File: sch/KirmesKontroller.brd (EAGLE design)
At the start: 100 x 80 mm, 31 parts, among them IC1 R-78E05-1.0, IC2 YB-ESP32-S3-AMP-V2, IC3 ULN2803, J1 MPE 087-1-003, X1 DG240 2,54-2, X2 DG240 2,54-2, X3 DG240 2,54-8, X4 DG240 2,54-8, X5 22-23-2031, X6 22-23-2031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

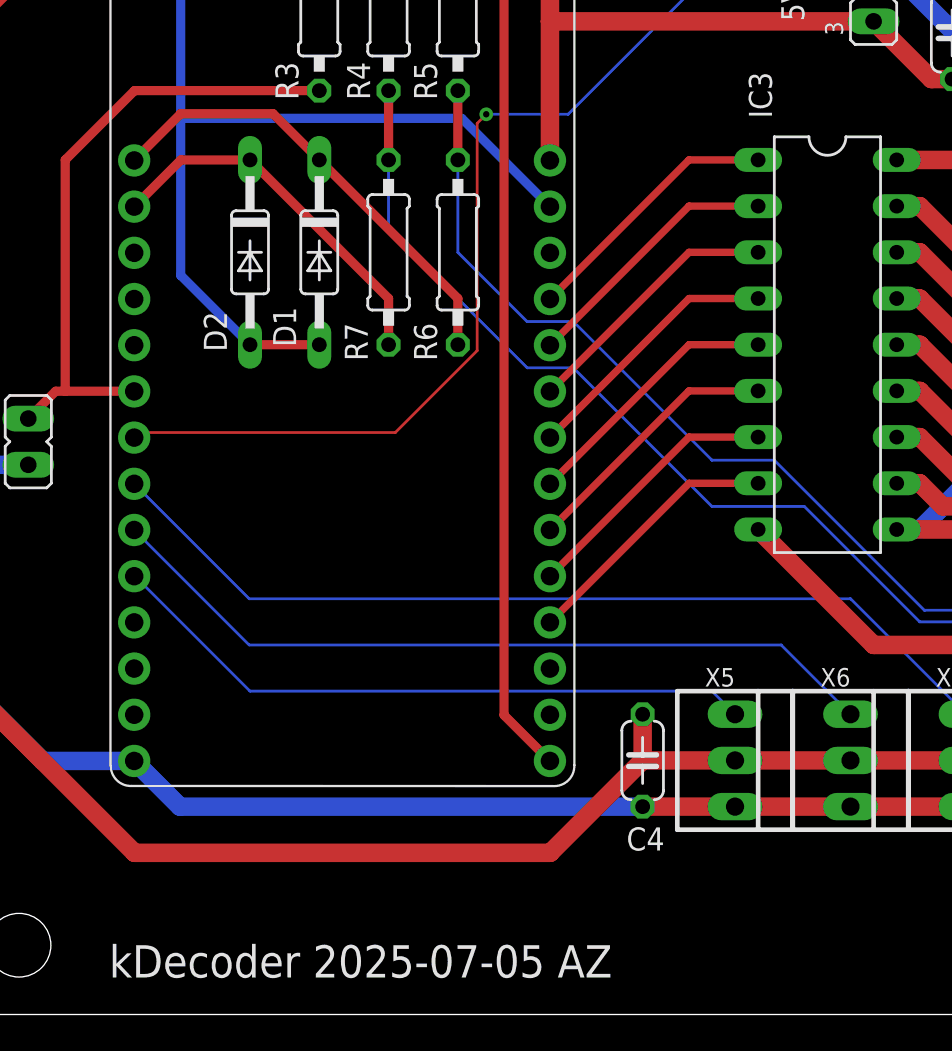
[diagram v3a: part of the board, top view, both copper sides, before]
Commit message: fixed pinmapping
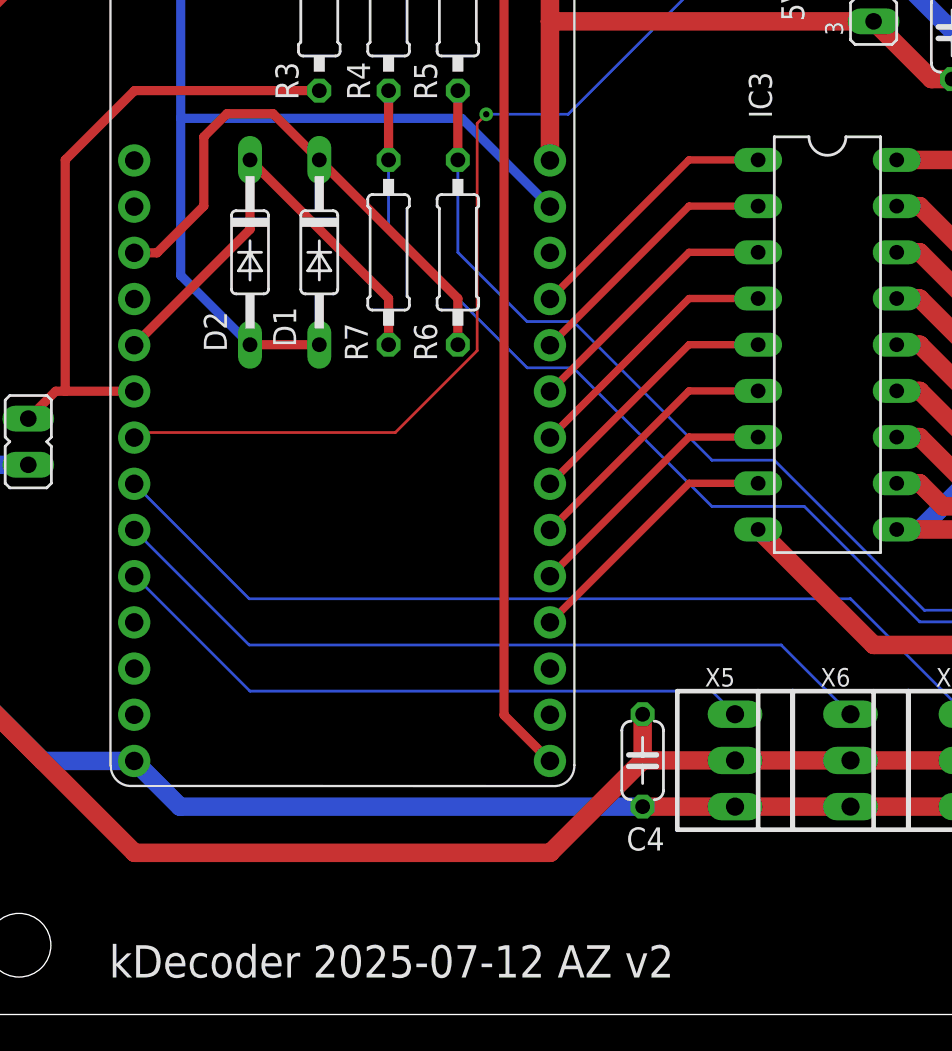
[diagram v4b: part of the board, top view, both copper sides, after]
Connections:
- net INPUT1: now also IC2.21; no longer IC2.47
- net INPUT2: now also IC2.38; no longer IC2.48
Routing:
- net INPUT2: track 20.7 -> 26.1 mm
- net INPUT1: track 25.6 -> 29.9 mm
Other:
- board text added: "kDecoder 2025-07-12 AZ v2"
- board text removed: "kDecoder 2025-07-05 AZ"
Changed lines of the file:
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@@
 <layers>
 <layer number="1" name="Top" color="4" fill="1" visible="yes" active="yes"/>
-<layer number="16" name="Bottom" color="1" fill="1" visible="yes" active="yes"/>
+<layer number="16" name="Bottom" color="1" fill="1" visible="no" active="yes"/>
 <layer number="17" name="Pads" color="2" fill="1" visible="yes" active="yes"/>
 <layer number="18" name="Vias" color="2" fill="1" visible="yes" active="yes"/>
@@
 <layer number="20" name="Dimension" color="24" fill="1" visible="yes" active="yes"/>
 <layer number="21" name="tPlace" color="7" fill="1" visible="yes" active="yes"/>
-<layer number="22" name="bPlace" color="7" fill="1" visible="yes" active="yes"/>
+<layer number="22" name="bPlace" color="7" fill="1" visible="no" active="yes"/>
 <layer number="23" name="tOrigins" color="15" fill="1" visible="yes" active="yes"/>
-<layer number="24" name="bOrigins" color="15" fill="1" visible="yes" active="yes"/>
+<layer number="24" name="bOrigins" color="15" fill="1" visible="no" active="yes"/>
 <layer number="25" name="tNames" color="7" fill="1" visible="yes" active="yes"/>
-<layer number="26" name="bNames" color="7" fill="1" visible="yes" active="yes"/>
+<layer number="26" name="bNames" color="7" fill="1" visible="no" active="yes"/>
 <layer number="27" name="tValues" color="7" fill="1" visible="no" active="yes"/>
 <layer number="28" name="bValues" color="7" fill="1" visible="no" active="yes"/>
@@
 <layer number="38" name="bTest" color="7" fill="1" visible="no" active="yes"/>
 <layer number="39" name="tKeepout" color="4" fill="11" visible="yes" active="yes"/>
-<layer number="40" name="bKeepout" color="1" fill="11" visible="yes" active="yes"/>
+<layer number="40" name="bKeepout" color="1" fill="11" visible="no" active="yes"/>
 <layer number="41" name="tRestrict" color="4" fill="10" visible="yes" active="yes"/>
-<layer number="42" name="bRestrict" color="1" fill="10" visible="yes" active="yes"/>
+<layer number="42" name="bRestrict" color="1" fill="10" visible="no" active="yes"/>
 <layer number="43" name="vRestrict" color="2" fill="10" visible="no" active="yes"/>
 <layer number="44" name="Drills" color="7" fill="1" visible="no" active="yes"/>
@@
 <layer number="50" name="dxf" color="7" fill="1" visible="no" active="no"/>
 <layer number="51" name="tDocu" color="7" fill="1" visible="yes" active="yes"/>
-<layer number="52" name="bDocu" color="7" fill="1" visible="yes" active="yes"/>
+<layer number="52" name="bDocu" color="7" fill="1" visible="no" active="yes"/>
 <layer number="53" name="tGND_GNDA" color="7" fill="9" visible="no" active="no"/>
 <layer number="54" name="bGND_GNDA" color="1" fill="9" visible="no" active="no"/>
@@
 <hole x="96.52" y="3.81" drill="3.5"/>
 <hole x="96.52" y="76.2" drill="3.5"/>
-<dimension x1="100" y1="80" x2="0" y2="80" x3="50" y3="83.82" textsize="1.778" layer="1"/>
-<dimension x1="0" y1="80" x2="0" y2="0" x3="-3.81" y3="40" textsize="1.778" layer="1"/>
-<text x="8.763" y="2.032" size="1.778" layer="25">kDecoder 2025-07-05 AZ</text>
+<dimension x1="100" y1="80" x2="0" y2="80" x3="50" y3="83.82" textsize="1.778" layer="20"/>
+<dimension x1="0" y1="80" x2="0" y2="0" x3="-3.81" y3="40" textsize="1.778" layer="20"/>
+<text x="8.763" y="2.032" size="1.778" layer="25">kDecoder 2025-07-12 AZ v2</text>
 <text x="46.99" y="57.15" size="1.27" layer="25" rot="R90">Vcc</text>
 <text x="46.99" y="54.61" size="1.27" layer="25" rot="R90">5V</text>
@@
 </signal>
 <signal name="INPUT2">
-<contactref element="IC2" pad="48"/>
 <contactref element="R7" pad="1"/>
 <contactref element="D2" pad="C"/>
-<wire x1="16.51" y1="46.99" x2="12.71125" y2="46.99" width="0.508" layer="1"/>
 <wire x1="16.51" y1="46.99" x2="24.13" y2="39.37" width="0.508" layer="1"/>
 <wire x1="24.13" y1="39.37" x2="24.13" y2="36.83" width="0.508" layer="1"/>
-<wire x1="12.71125" y1="46.99" x2="10.1425" y2="44.42125" width="0.508" layer="1"/>
+<contactref element="IC2" pad="38"/>
+<wire x1="10.1425" y1="36.80125" x2="16.51" y2="43.16875" width="0.508" layer="1"/>
+<wire x1="16.51" y1="43.16875" x2="16.51" y2="46.99" width="0.508" layer="1"/>
 </signal>
 <signal name="INPUT1">
-<contactref element="IC2" pad="47"/>
 <contactref element="R6" pad="1"/>
 <contactref element="D1" pad="C"/>
-<wire x1="12.7" y1="49.51875" x2="12.7" y2="49.53" width="0.508" layer="1"/>
-<wire x1="17.78" y1="49.53" x2="12.7" y2="49.53" width="0.508" layer="1"/>
-<wire x1="17.78" y1="49.53" x2="20.32" y2="46.99" width="0.508" layer="1"/>
 <wire x1="20.32" y1="46.99" x2="27.94" y2="39.37" width="0.508" layer="1"/>
 <wire x1="27.94" y1="39.37" x2="27.94" y2="36.83" width="0.508" layer="1"/>
-<wire x1="12.7" y1="49.53" x2="10.1425" y2="46.9725" width="0.508" layer="1"/>
-<wire x1="10.1425" y1="46.9725" x2="10.1425" y2="46.96125" width="0.508" layer="1"/>
+<contactref element="IC2" pad="21"/>
+<wire x1="20.32" y1="46.99" x2="17.78" y2="49.53" width="0.508" layer="1"/>
+<wire x1="17.78" y1="49.53" x2="15.24" y2="49.53" width="0.508" layer="1"/>
+<wire x1="15.24" y1="49.53" x2="13.97" y2="48.26" width="0.508" layer="1"/>
+<wire x1="13.97" y1="44.45" x2="11.40125" y2="41.88125" width="0.508" layer="1"/>
+<wire x1="11.40125" y1="41.88125" x2="10.1425" y2="41.88125" width="0.508" layer="1"/>
+<wire x1="13.97" y1="48.26" x2="13.97" y2="44.45" width="0.508" layer="1"/>
 </signal>
 <signal name="X3_B-8">

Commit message: pin 47 named
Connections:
- new net LED: IC2.47
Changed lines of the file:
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@@
 <wire x1="24.13" y1="43.18" x2="24.13" y2="46.99" width="0.1524" layer="16"/>
+</signal>
+<signal name="LED">
+<contactref element="IC2" pad="47"/>
 </signal>
 </signals>
